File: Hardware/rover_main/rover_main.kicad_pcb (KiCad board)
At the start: 2 copper layers, 85 x 70 mm, 36 parts, among them J1 BATT, J10 Analog, J2 BME280, J3 CSS811, J4 DRIVERS, J5 GY-87, J7 FTDI, J8 Digital, U1 LD1117A33, U2 MCP732831CHARGER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

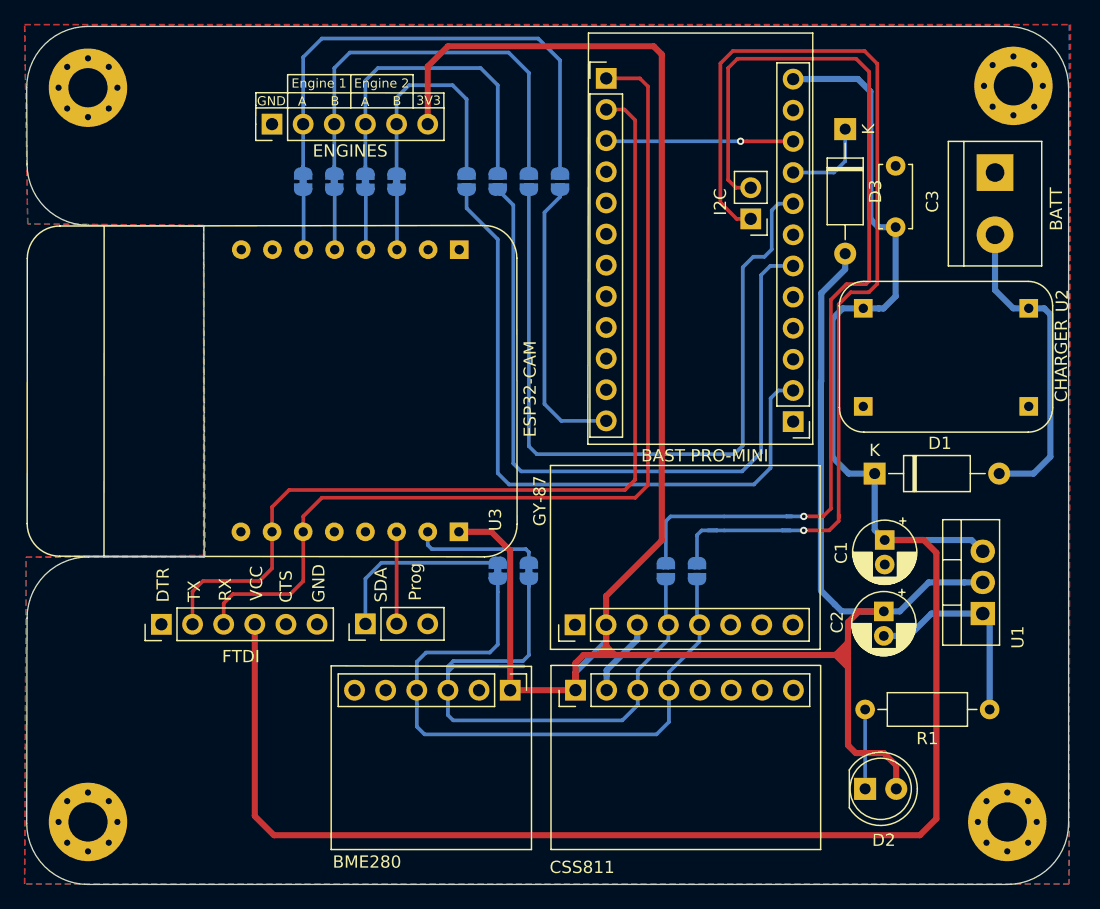
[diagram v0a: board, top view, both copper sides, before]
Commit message: Update traces and placement
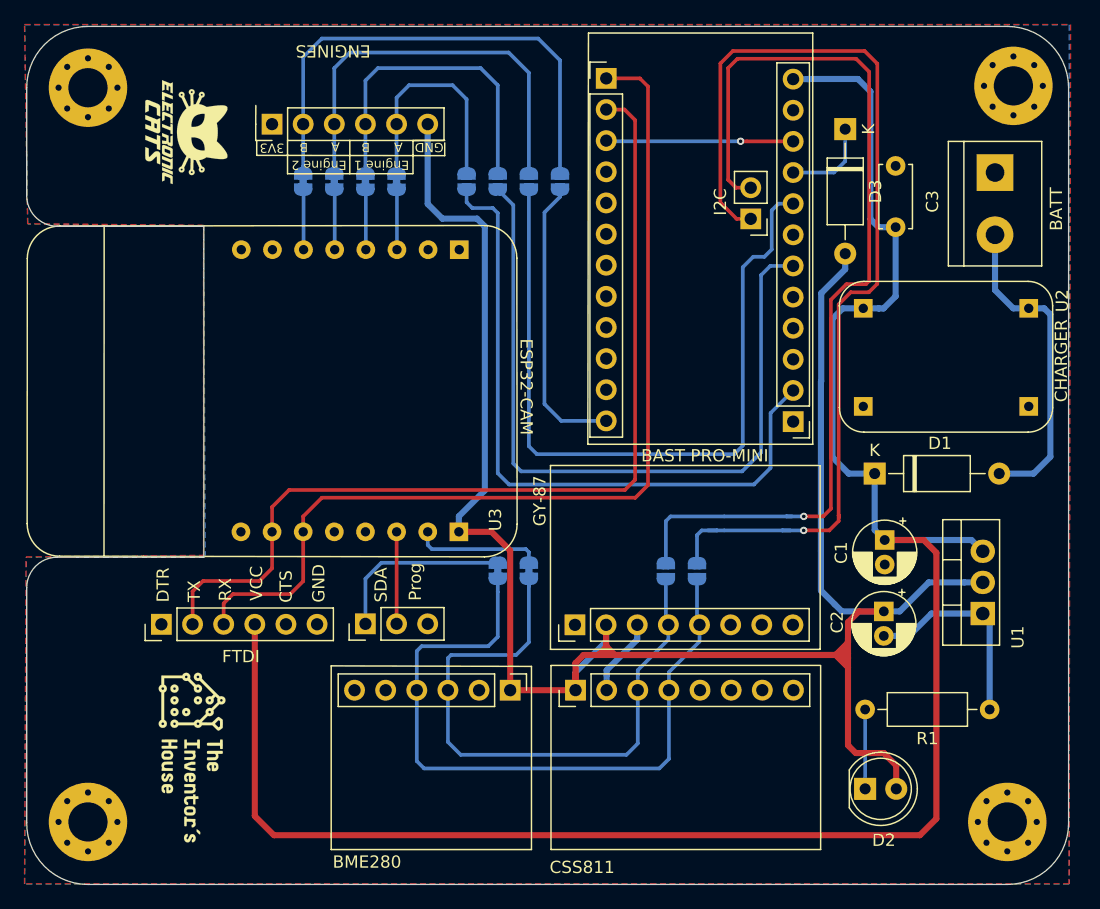
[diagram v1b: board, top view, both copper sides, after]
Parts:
- added G***: LOGO, Aesthetics:huntercat_135x74, F.Cu at (113.5, 119.8)
- added G***: LOGO, Aesthetics:electronic_cats_logo_8x6, F.Cu at (113.0, 68.7)
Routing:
- net +3V3: track 206.2 -> 170.8 mm
- net /SDA: track 51.7 -> 57.5 mm
- net /SCL: track 52.4 -> 49.8 mm
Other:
- outline, holes or cut-outs redrawn
- board text added: "DRIVERS BAST"
- board text added: "ESP32-CAM"
- board text removed: "DRIVERS BATS"

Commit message: move labels
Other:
- board text added: "+"
- board text added: "-"
- board text added: "BATT"
- board text added: "BME280"
- board text added: "BME280 TEMPERATURE HUMIDITY PRESSURE"
- board text added: "C1"
- board text added: "C2"
- board text added: "C3"
- board text added: "CSS811 AIR QUALITY *CO2 *VOC"
- board text added: "D3"
- board text added: "GY-87 ACCELETOMETER GYROSCOPE MAGNETOMETER DIGITAL PRESSURE"
- board text added: "K"
- board text added: "Prof"
- board text added: "REGULATOR"
- board text added: "SDA"
